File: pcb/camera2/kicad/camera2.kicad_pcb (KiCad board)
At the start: 4 copper layers, 96.5 x 45.7 mm, 28 parts

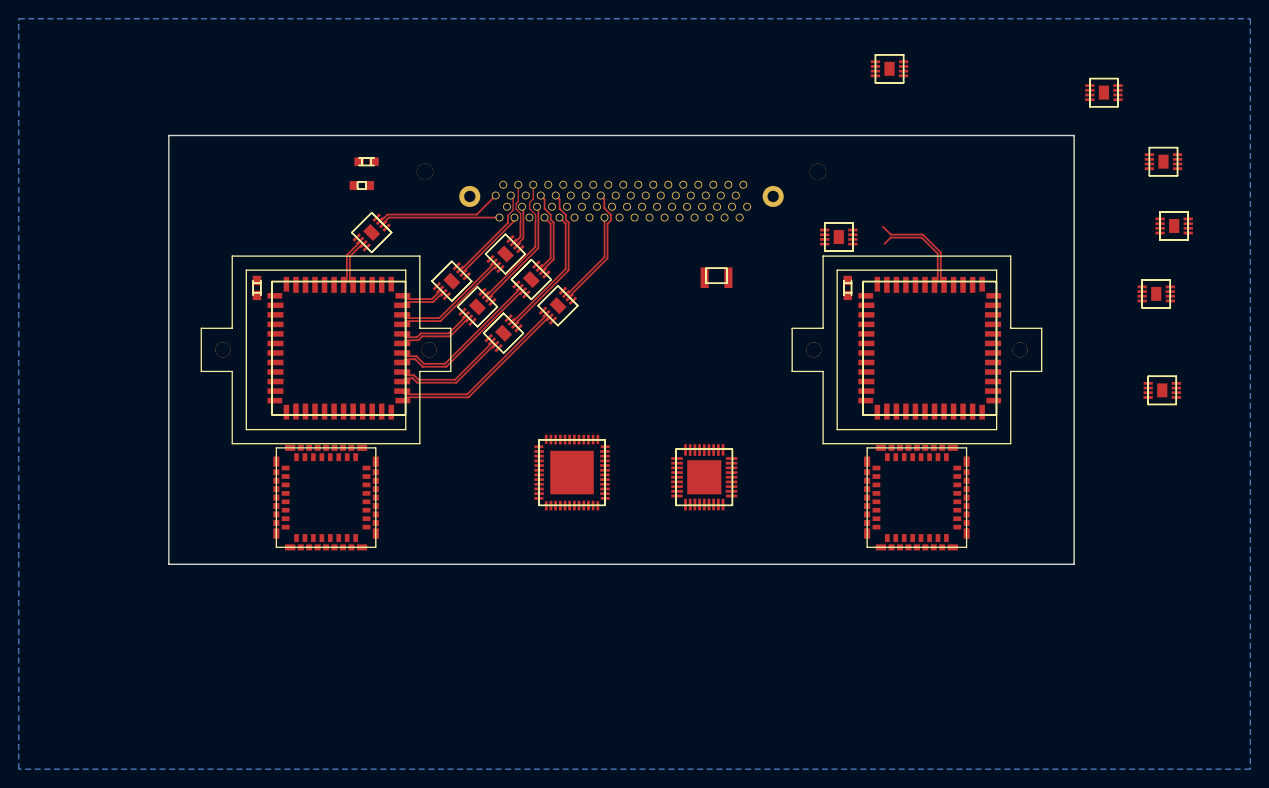
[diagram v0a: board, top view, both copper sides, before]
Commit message: camera pcb: finished routing differential pairs
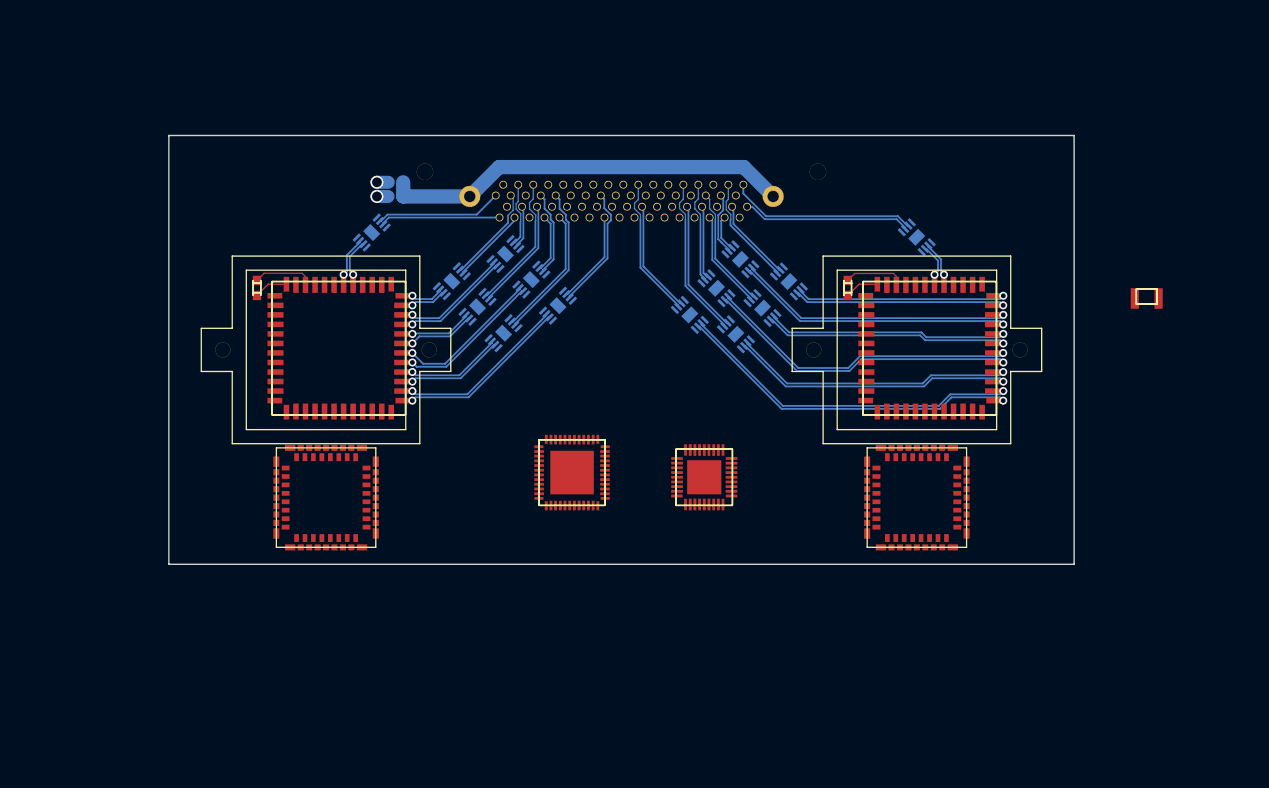
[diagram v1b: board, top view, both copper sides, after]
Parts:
- B1, B10, B11, B15, B16, B17, B18, B19, B2, B20, B3, B4, B5, B6: footprint gen:87275f9bd7c5351d5314038d0847896f97cccfc3388e99053950ee171f5369c6 -> gen:8b14518b2948365129873f979be7cb1c0b87a0d65ed63ad81105151247540314; moved to B.Cu
- C1U1, C2U1: footprint gen:d6a4e5e1732fb57863a7076c90e7bcf7410b0d66534498115b3786cec4b5a757 -> gen:6d493ddc3734994c4679d6f237aa2fb3f74991f820373e79c6f4096ba149339f
- C2, R2: moved to B.Cu
- U1: footprint gen:b209651823d3298e0e6eab7cce50a84d598caa6ee349ab7aa619ea57bf71a81e -> gen:8ab37654435c6d1db82287a4fc3d401412c641ce64f06749c2ba937c900847e4
- U2: footprint gen:e7440317a0065f9e5d349a45192785c649349203bd02b331def61b774a9908bf -> gen:dce4e3f8df3cb696cc9ab1a5e92b9530a765454f53e2929eb8d873347893b4de
- moved B18 46.4 mm to (162.5, 89.4), turned to 135 degrees
- moved B16 46.3 mm to (160.0, 92.5), turned to 135 degrees
- moved C1 45.9 mm to (205.9, 93.4)
- moved B17 45.5 mm to (164.9, 94.6), turned to 135 degrees
- moved B19 39.2 mm to (167.7, 91.8), turned to 135 degrees
- moved B11 33.8 mm to (157.2, 95.3), turned to 135 degrees
- moved B20 30.9 mm to (181.3, 87.0), turned to 315 degrees
- moved B15 15.1 mm to (162.1, 97.4), turned to 135 degrees
- moved R2 3.81 mm to (125.8, 81.2), turned to 180 degrees
- moved C2 3.80 mm to (125.8, 82.7), turned to 180 degrees
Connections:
- B1 pad 2: pair1P -> pair1N
- B1 pad 3: pair1N -> pair1P
- B1 pad 6: out1N -> out1P
- B1 pad 7: out1P -> out1N
- B10 pad 2: out10P -> out10N
- B10 pad 3: out10N -> out10P
- B10 pad 6: pair10N -> pair10P
- B10 pad 7: pair10P -> pair10N
- B15 pad 2: pair15P -> out15P
- B15 pad 3: pair15N -> out15N
- B15 pad 6: out15N -> pair15N
- B15 pad 7: out15P -> pair15P
- B17 pad 2: out17P -> out17N
- B17 pad 3: out17N -> out17P
- B17 pad 6: pair17N -> pair17P
- B17 pad 7: pair17P -> pair17N
- B2 pad 2: out2N -> out2P
- B2 pad 3: out2P -> out2N
- B2 pad 6: pair2P -> pair2N
- B2 pad 7: pair2N -> pair2P
- B20 pad 2: out20P -> pair20P
- B20 pad 3: out20N -> pair20N
- B20 pad 6: pair20N -> out20N
- B20 pad 7: pair20P -> out20P
- B3 pad 2: out3N -> out3P
- B3 pad 3: out3P -> out3N
- B3 pad 6: pair3P -> pair3N
- B3 pad 7: pair3N -> pair3P
- B4 pad 2: out4N -> out4P
- B4 pad 3: out4P -> out4N
- B4 pad 6: pair4P -> pair4N
- B4 pad 7: pair4N -> pair4P
- B5 pad 2: out5P -> out5N
- B5 pad 3: out5N -> out5P
- B5 pad 6: pair5N -> pair5P
- B5 pad 7: pair5P -> pair5N
- B6 pad 2: out6P -> out6N
- B6 pad 3: out6N -> out6P
- B6 pad 6: pair6N -> pair6P
- B6 pad 7: pair6P -> pair6N
- C2U1 pad 10: out16P -> out15P
- C2U1 pad 11: out17N -> out16N
- C2U1 pad 12: out17P -> out16P
- C2U1 pad 13: out18N -> out17P
- C2U1 pad 14: out18P -> out17N
- C2U1 pad 15: out19N -> out18N
- C2U1 pad 16: out19P -> out18P
- C2U1 pad 17: out20N -> out19N
- C2U1 pad 18: out20P -> out19P
- C2U1 pad 23: out15P -> out20N
- C2U1 pad 24: out15N -> out20P
- C2U1 pad 9: out16N -> out15N
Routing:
- net shield: track 0.00 -> 43.5 mm
- net out11N: track 0.00 -> 37.8 mm, vias 0 -> 1
- net out11P: track 0.00 -> 37.7 mm, vias 0 -> 1
- net out16N: track 0.00 -> 34.6 mm, vias 0 -> 1
- net out16P: track 0.00 -> 34.3 mm, vias 0 -> 1
- net out18N: track 0.00 -> 30.6 mm, vias 0 -> 1
- net out18P: track 0.00 -> 30.3 mm, vias 0 -> 1
- net out17P: track 0.00 -> 26.9 mm, vias 0 -> 1
- net out17N: track 0.00 -> 26.7 mm, vias 0 -> 1
- net out19N: track 0.00 -> 23.6 mm, vias 0 -> 1
- net out19P: track 0.00 -> 23.3 mm, vias 0 -> 1
- net out15N: track 10.1 -> 31.0 mm, vias 0 -> 1
- net pair20N: track 0.00 -> 20.0 mm
- net out15P: track 10.9 -> 30.7 mm, vias 0 -> 1
- net pair20P: track 0.00 -> 17.9 mm
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- added copper zone on In2.Cu, net gnd
- removed copper zone on B.Cu, net gnd
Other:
- board text added: "connect shield on top too!"
- board text removed: "make sure that LVDS pairs have ground plane on neighboring layer"

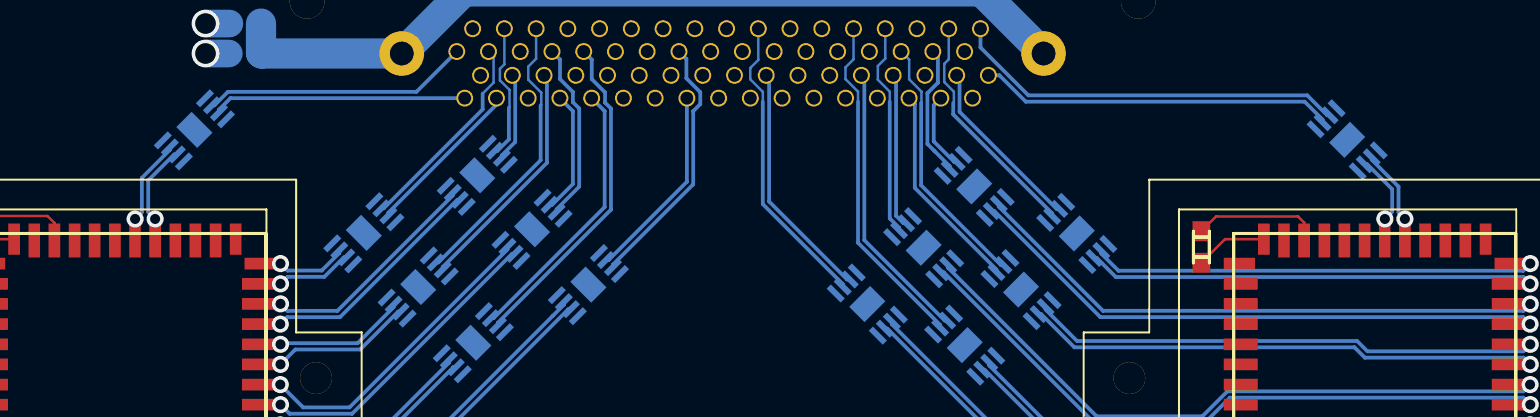
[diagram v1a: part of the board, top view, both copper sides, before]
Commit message: input termination
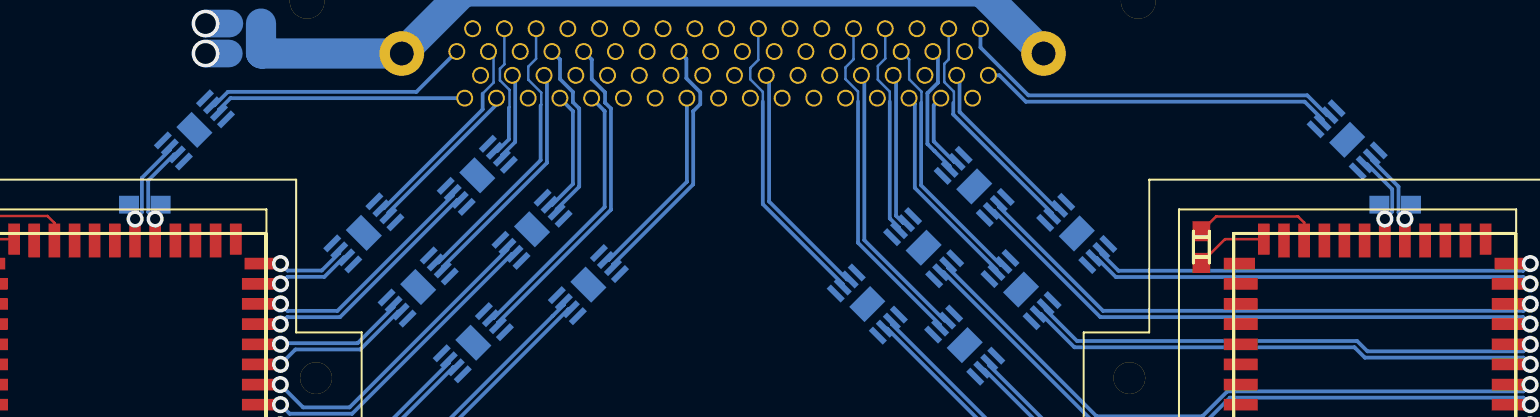
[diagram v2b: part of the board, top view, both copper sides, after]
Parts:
- added C1R2: , gen:57f8f96f6e6b2a00af4539d585b2f3bdc0d73935af5ecd13a4a5208aab3df262, B.Cu at (120.7, 90.3)
- added C2R2: , gen:57f8f96f6e6b2a00af4539d585b2f3bdc0d73935af5ecd13a4a5208aab3df262, B.Cu at (183.8, 90.3)
- B1, B10, B11, B15, B16, B17, B18, B19, B2, B20, B3, B4, B5, B6: footprint gen:8b14518b2948365129873f979be7cb1c0b87a0d65ed63ad81105151247540314 -> gen:cbfca23ea51b44d0e50a3924c338fdaf501ecf837853ca0935bf710595246917
- C1U1, C2U1: footprint gen:6d493ddc3734994c4679d6f237aa2fb3f74991f820373e79c6f4096ba149339f -> gen:5d1f1930f7c01770851f46e8351d4db1fd9f5c65118fd4a0a1e7ea98ff279bb1
- U1: footprint gen:8ab37654435c6d1db82287a4fc3d401412c641ce64f06749c2ba937c900847e4 -> gen:7b09ae1b7068efbb558ffcc33b7a57f5df1485786f8ffcf29869f699f75e23c2
- U2: footprint gen:dce4e3f8df3cb696cc9ab1a5e92b9530a765454f53e2929eb8d873347893b4de -> gen:2aade0dc8a5f8ebe5ecc55767e56888fa4e5b3aed246e7957621177410ec09fc
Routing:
- net out1N: track 5.42 -> 6.27 mm
- net out20N: track 4.88 -> 5.73 mm
- net out20P: track 4.65 -> 5.48 mm
- net out1P: track 5.16 -> 6.00 mm

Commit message: camera pcb: more work
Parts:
- added B10C: , gen:14fdd466f7178f17380f48cf89da463f18b4a0e8fcfb609cb3e620722c947cd3, B.Cu at (146.4, 92.6)
- added B11C: , gen:14fdd466f7178f17380f48cf89da463f18b4a0e8fcfb609cb3e620722c947cd3, B.Cu at (149.6, 72.3)
- added B15C: , gen:14fdd466f7178f17380f48cf89da463f18b4a0e8fcfb609cb3e620722c947cd3, B.Cu at (153.1, 72.3)
- added B16C: , gen:14fdd466f7178f17380f48cf89da463f18b4a0e8fcfb609cb3e620722c947cd3, B.Cu at (152.5, 67.3)
- added B17C: , gen:14fdd466f7178f17380f48cf89da463f18b4a0e8fcfb609cb3e620722c947cd3, B.Cu at (149.7, 67.4)
- added B18C: , gen:14fdd466f7178f17380f48cf89da463f18b4a0e8fcfb609cb3e620722c947cd3, B.Cu at (146.4, 67.3)
- added B19C: , gen:14fdd466f7178f17380f48cf89da463f18b4a0e8fcfb609cb3e620722c947cd3, B.Cu at (155.2, 67.4)
- added B1C: , gen:14fdd466f7178f17380f48cf89da463f18b4a0e8fcfb609cb3e620722c947cd3, B.Cu at (120.0, 88.3)
- added B20C: , gen:14fdd466f7178f17380f48cf89da463f18b4a0e8fcfb609cb3e620722c947cd3, B.Cu at (149.9, 70.8)
- added B2C: , gen:14fdd466f7178f17380f48cf89da463f18b4a0e8fcfb609cb3e620722c947cd3, F.Cu at (132.8, 91.7)
- added B3C: , gen:14fdd466f7178f17380f48cf89da463f18b4a0e8fcfb609cb3e620722c947cd3, B.Cu at (153.3, 70.7)
- added B4C: , gen:14fdd466f7178f17380f48cf89da463f18b4a0e8fcfb609cb3e620722c947cd3, B.Cu at (152.8, 69.0)
- added B5C: , gen:14fdd466f7178f17380f48cf89da463f18b4a0e8fcfb609cb3e620722c947cd3, B.Cu at (146.5, 68.9)
- added B6C: , gen:14fdd466f7178f17380f48cf89da463f18b4a0e8fcfb609cb3e620722c947cd3, B.Cu at (146.1, 70.5)
- added D0: , gen:c9b4f6ccae4bb0340b2ad5a6c71b1ffd2b7dd85978f603f30cef69603b532b8c, F.Cu at (106.6, 85.9)
- added D1: , gen:c9b4f6ccae4bb0340b2ad5a6c71b1ffd2b7dd85978f603f30cef69603b532b8c, F.Cu at (106.6, 112.3)
- added D2: , gen:c9b4f6ccae4bb0340b2ad5a6c71b1ffd2b7dd85978f603f30cef69603b532b8c, F.Cu at (193.1, 112.3)
- added D3: , gen:c9b4f6ccae4bb0340b2ad5a6c71b1ffd2b7dd85978f603f30cef69603b532b8c, F.Cu at (193.1, 85.9)
- added M0: , gen:3c7f55a43bbd183404c5b8309475486c24daf5a9c2963092a0b256ddf24e95e1, F.Cu at (105.1, 79.5)
- added M1: , gen:3c7f55a43bbd183404c5b8309475486c24daf5a9c2963092a0b256ddf24e95e1, F.Cu at (105.4, 118.1)
- added M2: , gen:3c7f55a43bbd183404c5b8309475486c24daf5a9c2963092a0b256ddf24e95e1, F.Cu at (194.3, 118.1)
- added M3: , gen:3c7f55a43bbd183404c5b8309475486c24daf5a9c2963092a0b256ddf24e95e1, F.Cu at (194.3, 80.0)
- added REG0: , gen:a8a9fe32768e32ddc75aa8295cef6929db764d9ac77e4627a54db0fef3c1f31a, F.Cu at (141.0, 100.9)
- added REG1: , gen:0ebfd6ab58889eb03d8f26c7dd1b53306c9215b0059415f86bfdbb9abe3fdde1, F.Cu at (141.8, 119.5)
- added REG2: , gen:eb209b2e1d221af71ed48e28bfe0bb8298d616a411442e29f3453ccc73495e89, F.Cu at (159.4, 103.5)
- added REG3: , gen:5bda942c242ea2bebc3cf29ef5f6c3ab9ee59d551a6204d93c9eca0998310be8, F.Cu at (162.0, 119.2)
- B1, B10, B11, B15, B16, B17, B18, B19, B2, B20, B3, B4, B5, B6: footprint gen:cbfca23ea51b44d0e50a3924c338fdaf501ecf837853ca0935bf710595246917 -> gen:b84940fdfb16a2d7942b3b406dd98b10c2c2213999c6866e353299b244b8fc6e
- C1U1, C2U1: footprint gen:5d1f1930f7c01770851f46e8351d4db1fd9f5c65118fd4a0a1e7ea98ff279bb1 -> gen:c58747e0684f9d36f894e920eb782c552f159bd2e92cf7dd16541e289be4d654
- U1: footprint gen:7b09ae1b7068efbb558ffcc33b7a57f5df1485786f8ffcf29869f699f75e23c2 -> gen:2f9b442f54b7add4956d34ec651f64beab61546dadc67e38d2c3fc0b09ac9096; moved to B.Cu
- U2: footprint gen:2aade0dc8a5f8ebe5ecc55767e56888fa4e5b3aed246e7957621177410ec09fc -> gen:cf96d1af73b58f8f1f3d64f5194d5234fe541250e2558da2cd5d85457dfd18e6
- moved U2 15.3 mm to (149.9, 97.8)
- moved U1 5.71 mm to (153.6, 110.0)
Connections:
- net vcc5 renamed vcc5in
- B1 pad 8: vcc3_3 -> vcc3_3in
- B10 pad 8: vcc3_3 -> vcc3_3in
- B11 pad 8: vcc3_3 -> vcc3_3in
- B15 pad 8: vcc3_3 -> vcc3_3in
- B16 pad 8: vcc3_3 -> vcc3_3in
- B17 pad 8: vcc3_3 -> vcc3_3in
- B18 pad 8: vcc3_3 -> vcc3_3in
- B19 pad 8: vcc3_3 -> vcc3_3in
- B2 pad 8: vcc3_3 -> vcc3_3in
- B20 pad 8: vcc3_3 -> vcc3_3in
- B3 pad 8: vcc3_3 -> vcc3_3in
- B4 pad 8: vcc3_3 -> vcc3_3in
- B5 pad 8: vcc3_3 -> vcc3_3in
- B6 pad 8: vcc3_3 -> vcc3_3in
- C1 pad 1: vcc3_3 -> vcc3_0
- C1U1 pad 1: vcc3_3 -> vcc3_0
- C1U1 pad 19: vcc3_3 -> vcc3_0
- C1U1 pad 29: vcc3_3 -> vcc3_0
- C1U1 pad 31: vcc3_3 -> vcc3_0
- C1U1 pad 33: vcc3_3 -> vcc3_0
- C1U1 pad 36: vcc3_3 -> vcc3_0
- C1U1 pad 38: vcc3_3 -> vcc3_0
- C1U1 pad 40: vcc3_3 -> vcc3_0
- C2U1 pad 1: vcc3_3 -> vcc3_0
- C2U1 pad 19: vcc3_3 -> vcc3_0
- C2U1 pad 29: vcc3_3 -> vcc3_0
- C2U1 pad 31: vcc3_3 -> vcc3_0
- C2U1 pad 33: vcc3_3 -> vcc3_0
- C2U1 pad 36: vcc3_3 -> vcc3_0
- C2U1 pad 38: vcc3_3 -> vcc3_0
- C2U1 pad 40: vcc3_3 -> vcc3_0
- P1 pad 16: P1_16 -> vcc3_3in
- P1 pad 19: P1_19 -> vcc3_3in
- P1 pad 50: P1_50 -> vcc3_3in
- P1 pad 53: P1_53 -> vcc3_3in
- T1 pad 16: vcc2_8 -> vcc3_0
- T2 pad 16: vcc2_8 -> vcc3_0
- U1 pad 1: vcc3_3 -> vcc3_0
- U1 pad 19: vcc3_3 -> vcc3_0
- U1 pad 27: vcc3_3 -> vcc3_0
- U1 pad 4: vcc3_3 -> vcc3_0
- U2 pad 19: U2_19 -> vcc3_0
- U2 pad 3: U2_3 -> vcc3_0
- U2 pad 42: U2_42 -> vcc3_0
- U2 pad P: U2_P -> gnd
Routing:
- net gnd: track 9.66 -> 15.0 mm, vias 2 -> 7
- net vcc3_0: track 0.00 -> 2.94 mm, vias 0 -> 3
- net vcc1_8: track 0.00 -> 2.17 mm, vias 0 -> 2
- net out11P: track 37.7 -> 37.0 mm
- net out11N: track 37.8 -> 37.1 mm
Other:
- board text added: "1.2"
- board text added: "2.8"
